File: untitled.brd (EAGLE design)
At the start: 51.3 x 48.9 mm, 11 parts, among them IC1 STM32F030F4P, U1 GY-521MPU6050, X1 332-02, X2 332-04, X3 332-02, X4 332-02, X5 332-02

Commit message: version 0.3 - proto 1
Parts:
- removed U$2: RFM69, RFM69mod:20X16BOARD
- removed X1, X3, X4, X5: 332-02, con-garry:332-02
- removed X2: 332-04, con-garry:332-04
- added JP1: (no value), pinhead:2X02
- added JP2, JP3, JP4, JP5: (no value), pinhead:1X02
- added U2: RFM69CW, mike-temp:RFM69CW-XXXS2
- moved U1 6.71 mm to (70.4, 30.7), turned to 0 degrees
- moved R1 1.52 mm to (16.8, 34.8)
- moved R2 0.76 mm to (14.2, 34.8)
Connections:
- removed net N$5: IC1.12, U$2.MISO
- removed net NC: U$2.NC
- new net N$13: IC1.11, U2.6
- net GND: now also JP1.2, JP2.2, JP5.1, U2.14, U2.3; no longer U$2.GND@1, U$2.GND@2, X1.2, X2.2, X5.1
- net N$10: now also JP5.2; no longer X5.2
- net N$11: now also JP3.2; no longer X4.1
- net N$2: now also JP1.1; no longer X2.1
- net N$3: now also IC1.12, U2.8; no longer IC1.11, U$2.SCK
- net N$4: now also U2.7; no longer U$2.NSS
- net N$6: now also U2.5; no longer U$2.MOSI
- net N$7: now also JP1.3; no longer X2.3
- net N$8: now also JP4.1; no longer X3.1
- net N$9: now also JP4.2; no longer X3.2
- net VCC: now also JP1.4, JP2.1, JP3.1, U2.2; no longer U$2.3.3V, X1.1, X2.4, X4.2
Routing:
- net GND: track 71.7 -> 27.0 mm
- net N$3: track 14.4 -> 0.00 mm
- net N$5: track 13.5 -> 0.00 mm
- net N$1: track 5.09 -> 7.54 mm
- net N$4: track 39.3 -> 41.6 mm
- net VCC: track 64.4 -> 66.6 mm
- net N$10: track 14.3 -> 15.7 mm
- net N$11: track 2.54 -> 3.36 mm

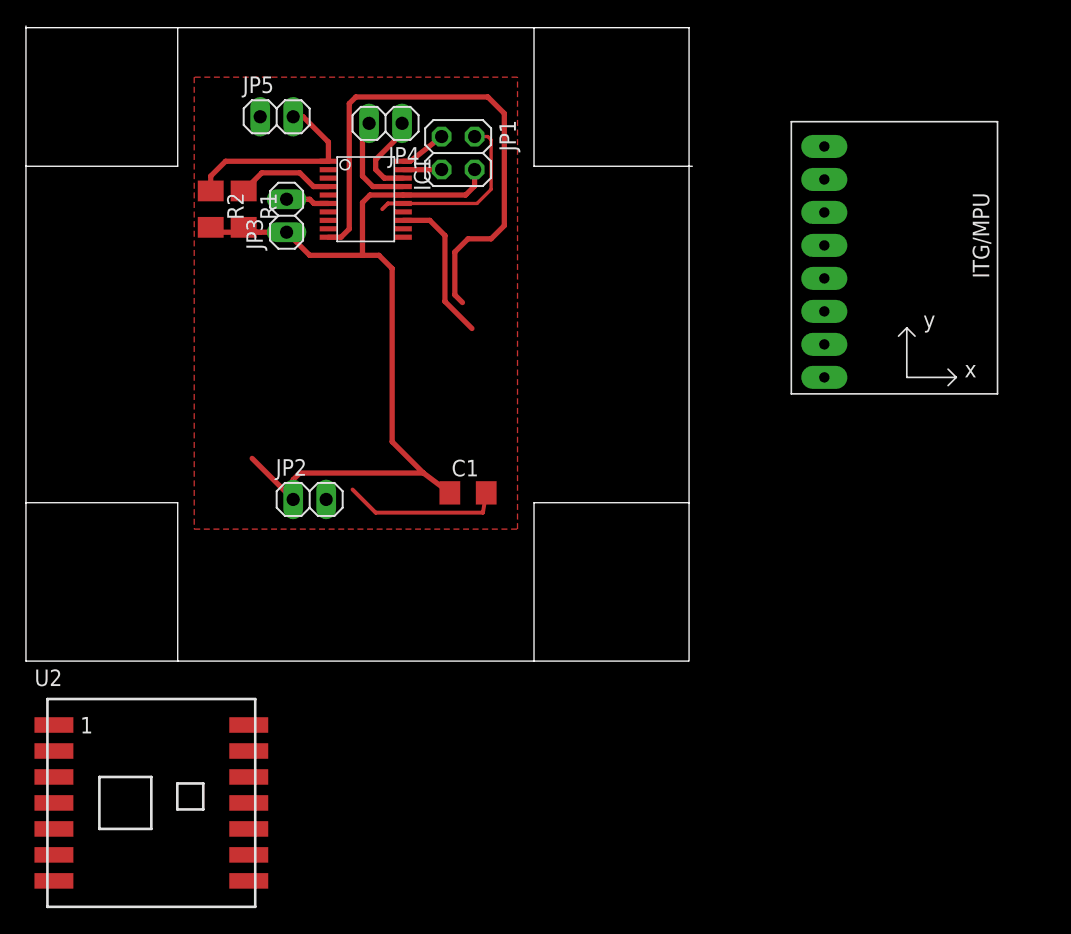
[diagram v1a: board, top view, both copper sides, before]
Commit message: Change MCU to bigger version
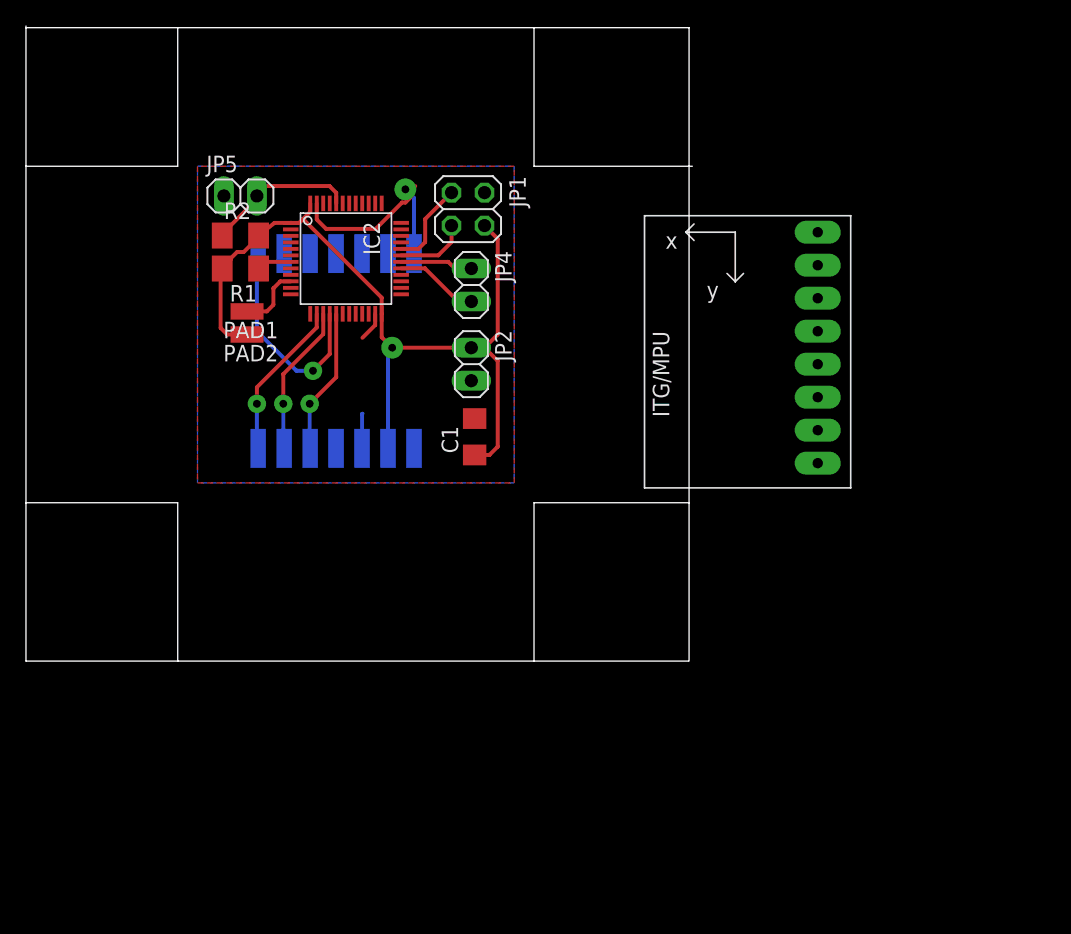
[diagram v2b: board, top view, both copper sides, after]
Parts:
- removed IC1: STM32F030F4P, micro-stm_v2:TSSOP20-I
- removed JP3: (no value), pinhead:1X02
- added IC2: STM32F030C8T, micro-stm_v2:LQFP48
- added PAD1, PAD2: (no value), wirepad:SMD1,27-2,54
- moved U2 37.6 mm to (23.9, 23.9), flipped to the bottom, turned to 90 degrees
- moved U1 19.4 mm to (52.1, 24.1), turned to 180 degrees
- moved JP2 16.2 mm to (34.3, 22.9), turned to 270 degrees
- moved JP4 14.1 mm to (34.3, 29.0), turned to 270 degrees
- moved JP5 6.71 mm to (16.5, 35.8)
- moved R1 4.58 mm to (16.5, 30.2), turned to 180 degrees
- moved JP1 4.38 mm to (34.0, 34.8)
- moved C1 4.35 mm to (34.5, 17.3), turned to 90 degrees
- moved R2 3.06 mm to (16.5, 32.8), turned to 0 degrees
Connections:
- new net VSSA: IC2.8
- net GND: now also IC2.23, IC2.47; no longer IC1.15
- net N$1: now also IC2.7; no longer IC1.4
- net N$10: now also IC2.44; no longer IC1.1
- net N$11: now also IC2.10, PAD1.1; no longer IC1.6, JP3.2
- net N$13: now also IC2.15; no longer IC1.11
- net N$2: now also IC2.32; no longer IC1.20
- net N$3: now also IC2.16; no longer IC1.12
- net N$4: now also IC2.14; no longer IC1.10
- net N$6: now also IC2.17; no longer IC1.13
- net N$7: now also IC2.31; no longer IC1.19
- net N$8: now also IC2.30; no longer IC1.18
- net N$9: now also IC2.29; no longer IC1.17
- net VCC: now also IC2.1, IC2.24, IC2.48, PAD2.1; no longer IC1.16, JP3.1
- net VDDA: now also IC2.9; no longer IC1.5
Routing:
- net N$4: track 41.6 -> 13.5 mm, vias 0 -> 1
- net N$3: track 0.00 -> 16.5 mm, vias 0 -> 1
- net N$13: track 0.00 -> 12.8 mm, vias 0 -> 1
- net GND: track 27.0 -> 20.9 mm, vias 0 -> 1
- net N$1: track 7.54 -> 2.99 mm
- net N$10: track 15.7 -> 12.3 mm
- net N$2: track 3.63 -> 6.71 mm
- net N$7: track 2.97 -> 5.57 mm
- net N$11: track 3.36 -> 5.07 mm
- net VCC: track 66.6 -> 65.0 mm, vias 0 -> 1
- net N$9: track 7.74 -> 6.46 mm
- net N$8: track 6.78 -> 5.61 mm
- net N$6: track 11.7 -> 12.3 mm, vias 0 -> 1
- added copper zone on layer 16, net GND

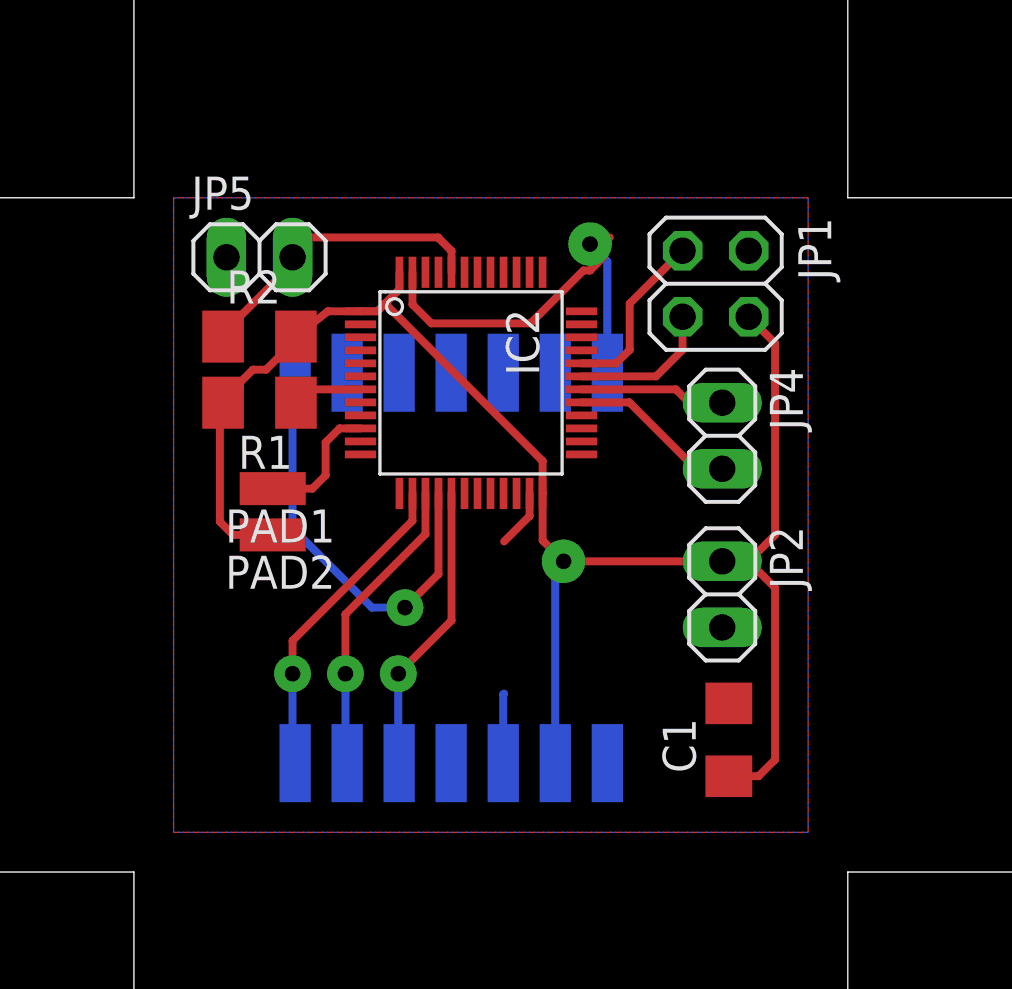
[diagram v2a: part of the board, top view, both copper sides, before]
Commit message: Fix jtag pins
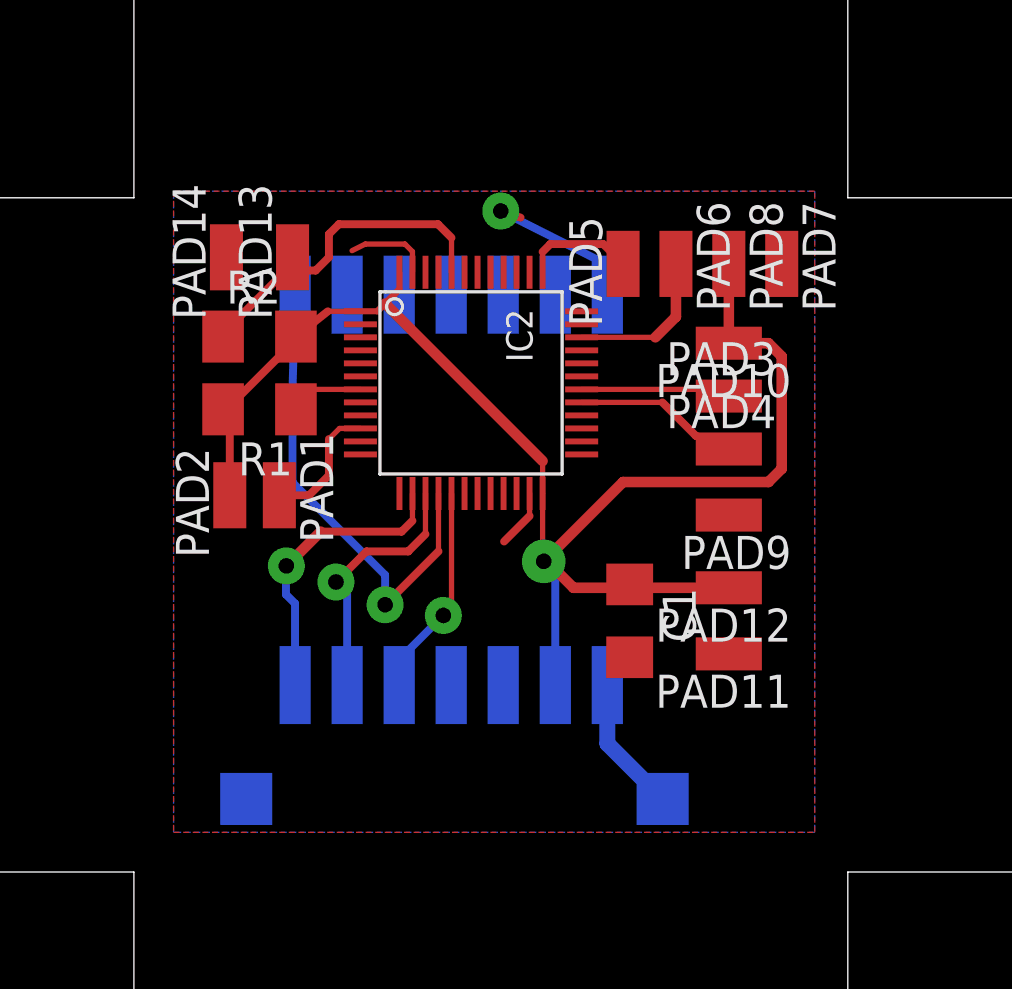
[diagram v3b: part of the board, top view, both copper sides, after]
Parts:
- removed JP1: (no value), pinhead:2X02
- removed JP2, JP4, JP5: (no value), pinhead:1X02
- added PAD10, PAD11, PAD12, PAD13, PAD14, PAD3, PAD4, PAD5, PAD6, PAD7, PAD8, PAD9: (no value), wirepad:SMD1,27-2,54
- added TP1, TP2: TPSQTP20SQ, testpad:TP20SQ
- moved C1 5.95 mm to (30.7, 21.8), turned to 270 degrees
- moved U2 3.00 mm to (23.9, 26.9)
- moved PAD2 2.25 mm to (15.4, 26.7), turned to 0 degrees
- moved PAD1 0.36 mm to (17.3, 26.7), turned to 180 degrees
- moved R1 0.25 mm to (16.5, 30.0)
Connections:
- new net N$5: TP2.TP, U2.1
- net GND: now also PAD11.1, PAD14.1, PAD7.1, PAD9.1; no longer JP1.2, JP2.2, JP5.1
- net N$10: now also PAD13.1; no longer JP5.2
- net N$2: now also IC2.37, PAD5.1; no longer IC2.32, JP1.1
- net N$7: now also IC2.34, PAD6.1; no longer IC2.31, JP1.3
- net N$8: now also PAD3.1; no longer JP4.1
- net N$9: now also PAD4.1; no longer JP4.2
- net VCC: now also PAD10.1, PAD12.1, PAD8.1; no longer JP1.4, JP2.1
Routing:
- net GND: track 20.9 -> 12.6 mm
- net N$5: track 0.00 -> 5.26 mm
- net VCC: track 65.0 -> 60.0 mm
- net N$6: track 12.3 -> 8.20 mm
- net N$13: track 12.8 -> 9.90 mm
- net N$4: track 13.5 -> 11.3 mm
- net N$3: track 16.5 -> 18.5 mm
- net N$2: track 6.71 -> 4.77 mm
- net N$10: track 12.3 -> 13.1 mm

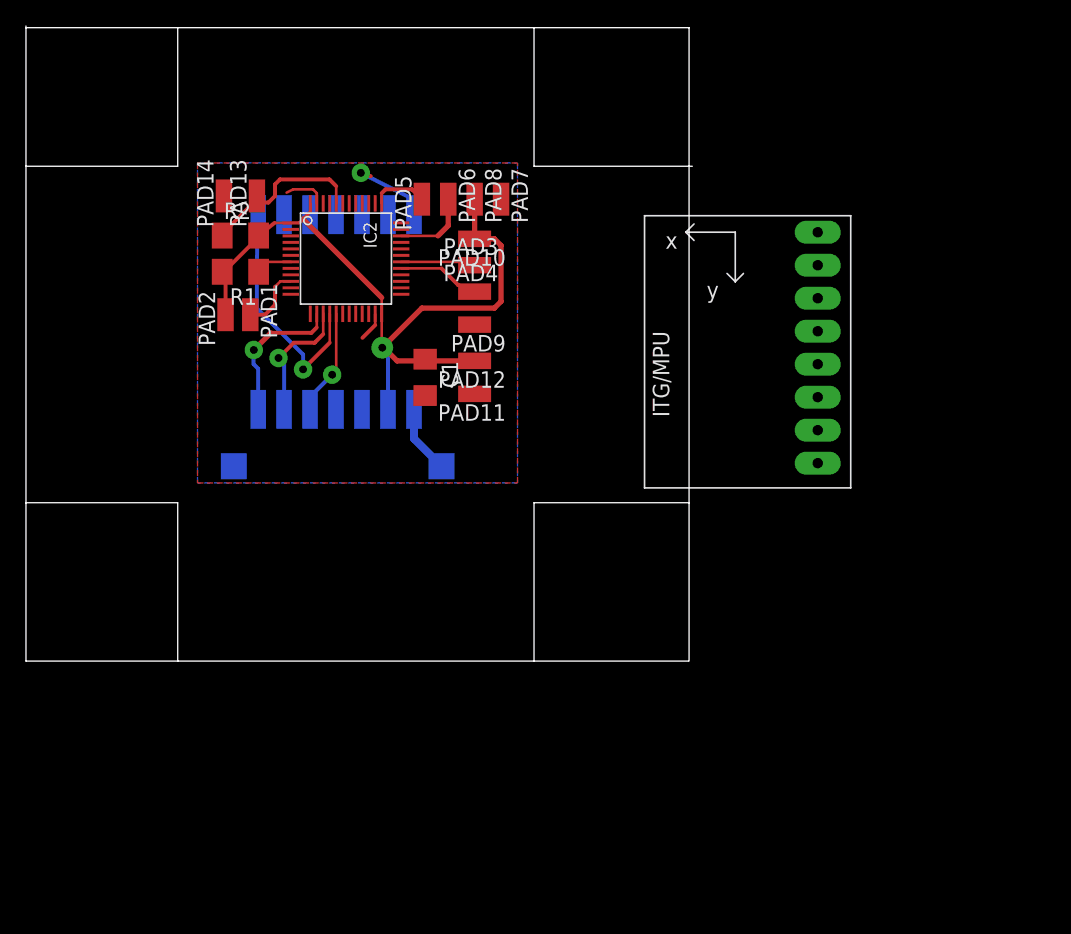
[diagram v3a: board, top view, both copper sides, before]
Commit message: Fix usasrt/i2c pins
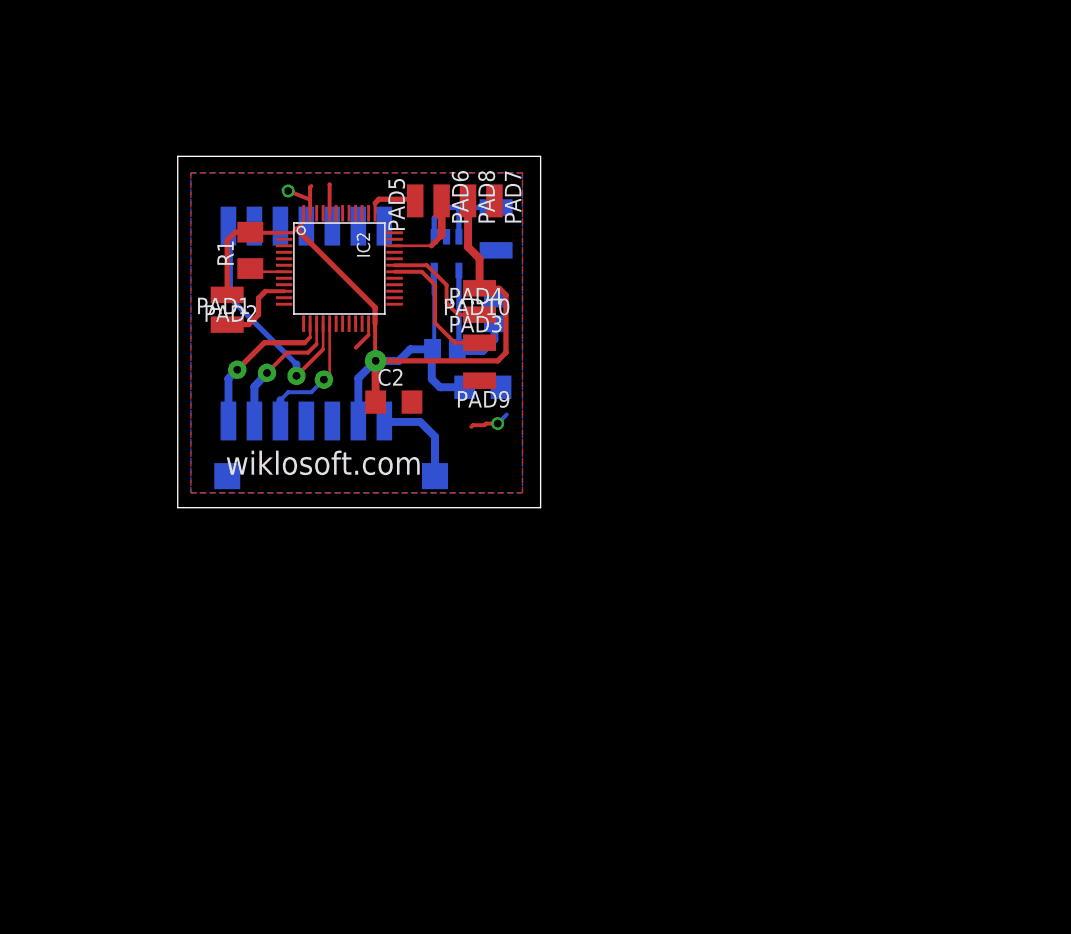
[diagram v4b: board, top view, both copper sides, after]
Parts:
- removed PAD13, PAD14: (no value), wirepad:SMD1,27-2,54
- removed R2: (no value), rcl:M1206
- removed U1: GY-521MPU6050, gy-521:GY-521
- added C2: (no value), rcl:C1206
- added IC1: TPS77015, texas:SOT23-DBV
- added R3, R4: (no value), rcl:M0805
- moved PAD12 11.9 mm to (36.2, 34.9), flipped to the bottom, turned to 270 degrees
- moved PAD11 11.2 mm to (36.2, 31.6), flipped to the bottom, turned to 270 degrees
- moved PAD3 5.98 mm to (34.9, 24.5)
- moved C1 4.51 mm to (35.2, 21.1), flipped to the bottom, turned to 180 degrees
- moved PAD9 4.33 mm to (34.9, 21.6)
- moved PAD10 3.83 mm to (34.9, 28.7)
- moved U2 2.45 mm to (21.6, 26.0)
- moved PAD1 1.93 mm to (15.5, 25.9), turned to 270 degrees
- moved PAD4 1.82 mm to (34.9, 26.7)
- moved R1 1.82 mm to (17.3, 31.6), turned to 90 degrees
- moved PAD2 1.53 mm to (15.5, 28.2), turned to 90 degrees
- moved IC2 0.92 mm to (24.1, 30.2)
- moved TP1 0.92 mm to (15.5, 14.2)
- moved TP2 0.92 mm to (31.5, 14.2)
- moved PAD6 0.52 mm to (32.0, 35.4)
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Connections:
- removed net N$10: IC2.44, PAD13.1, R2.1
- new net N$12: IC1.1, IC1.3, PAD12.1
- new net N$14: IC1.4, R3.1, R4.2
- net GND: now also C2.2, IC1.2, IC2.44, R4.1; no longer PAD14.1
- net N$9: now also IC2.31; no longer IC2.29
- net VCC: now also C2.1, IC1.5, R3.2; no longer PAD12.1, R2.2
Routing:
- net N$10: track 13.1 -> 0.00 mm
- net VCC: track 60.0 -> 72.4 mm
- net N$14: track 0.00 -> 10.6 mm
- net N$12: track 0.00 -> 8.87 mm
- net N$8: track 5.91 -> 10.5 mm
- net N$9: track 6.28 -> 8.94 mm
- net N$5: track 5.26 -> 7.44 mm
- net N$6: track 8.20 -> 10.1 mm
- net N$11: track 5.00 -> 6.19 mm
- net N$4: track 11.3 -> 12.1 mm
- net N$7: track 5.98 -> 6.62 mm
- net GND: track 12.6 -> 12.0 mm, vias 1 -> 2
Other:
- board size 51.3 x 48.9 mm -> 27.9 x 27.1 mm
- board text added: "wiklosoft.com"
